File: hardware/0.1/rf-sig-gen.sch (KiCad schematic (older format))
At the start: 89 parts, among them J1 Feather, J2 SMA, U1 MAX2871, U2 LP5912, U3 MIC5366-1.8, U4 SKY12347-362LF, U5 TRF37A75, U6 AD8319, U7 STP08CP05

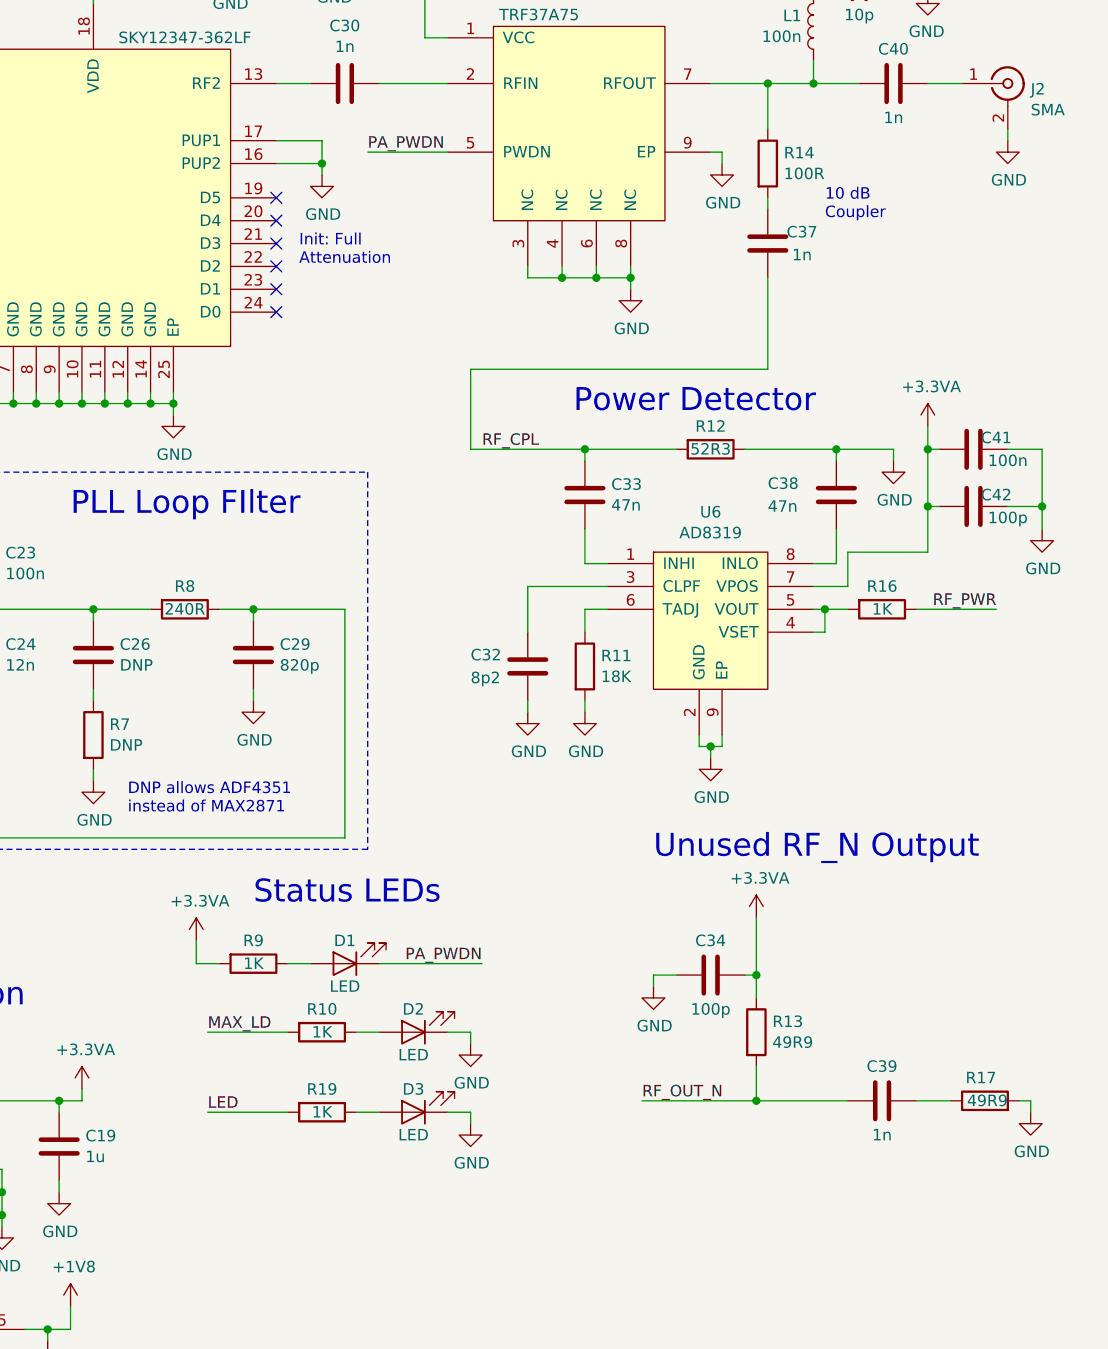
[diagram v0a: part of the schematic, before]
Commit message: update schematic
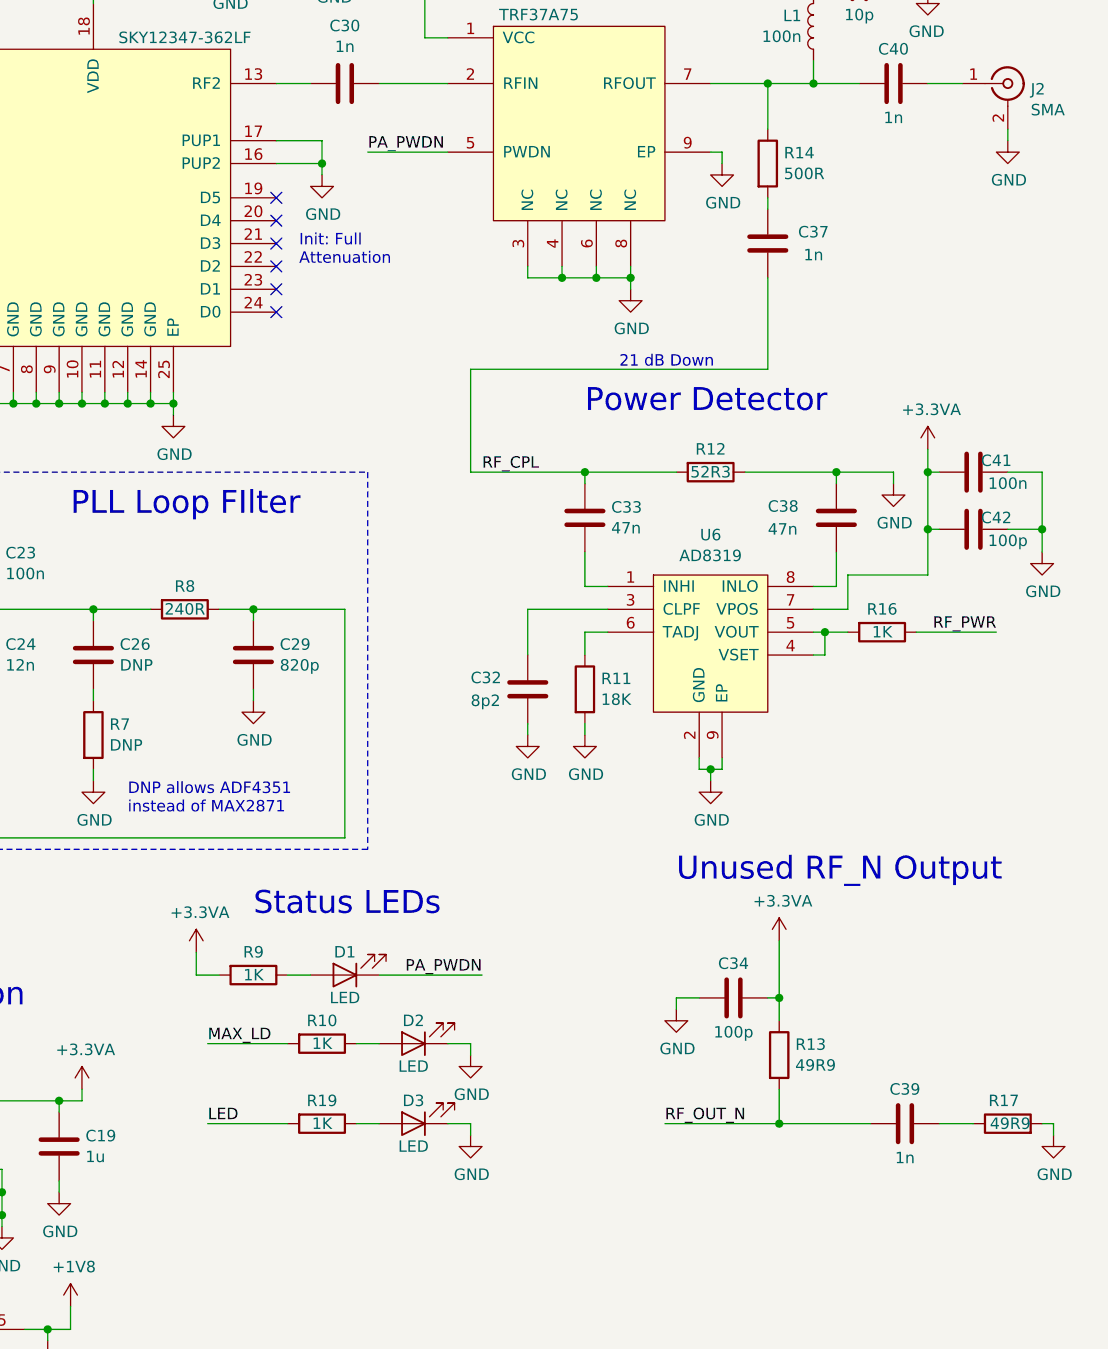
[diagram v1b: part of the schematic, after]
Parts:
- R14: value 100R -> 500R
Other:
- note added: "21 dB Down"
- note removed: "10 dB \nCoupler"
- moved on the sheet: C32, C33, C34, C38, C39, C41, C42, D1, D2, D3, R10, R11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
